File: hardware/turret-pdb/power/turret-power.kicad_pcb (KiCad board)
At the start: 2 copper layers, 70 x 68 mm, 21 parts, among them J1 Battery in, J10 Vision 5V, J11 Servo bus 7.5V, J12 Stack link, J2 12V bench, J3 Arm switch, J4 Pusher, U3 MP1584 7.5V, U4 MP1584 6V, U5 MP1584 5V

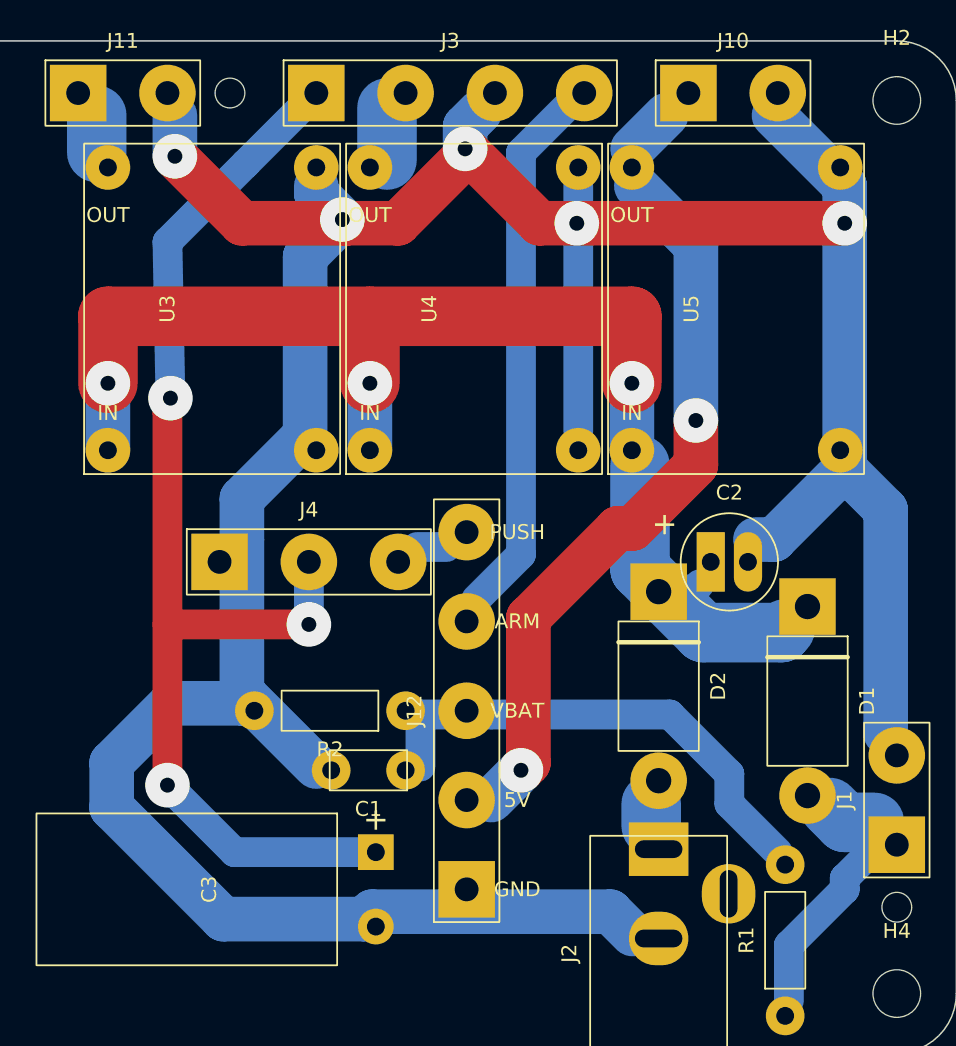
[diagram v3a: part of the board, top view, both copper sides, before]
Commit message: Move C2 off D2's cathode and give J4 room from the link pads
Co-Authored-By: Claude Opus 5.5 <noreply@anthropic.com>
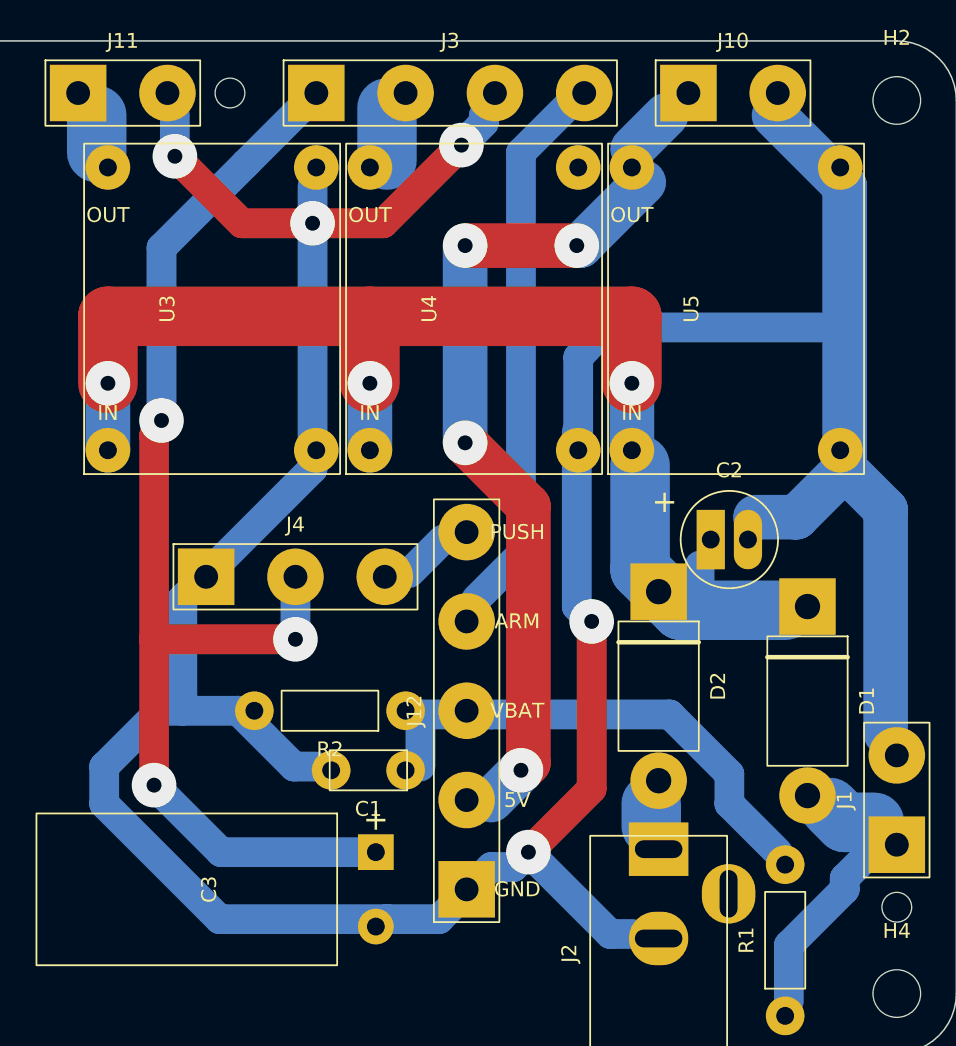
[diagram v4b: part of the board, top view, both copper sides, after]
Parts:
- moved C2 1.50 mm to (93.5, 73.5)
- moved J4 1.35 mm to (59.6, 76.0)
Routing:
- net GND: track 223.9 -> 236.4 mm
- net +5V: track 52.4 -> 57.0 mm, vias 2 -> 4
- net PUSH_SIG: track 2.00 -> 3.18 mm
- net PUSH_6V: track 80.2 -> 81.4 mm
